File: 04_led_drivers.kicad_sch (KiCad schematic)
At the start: 22 parts, among them Q4 AO3401A (30V Vds, satisfies b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, Q5 AO3401A (30V Vds, satisfies b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, U5 LM3409HVMY/NOPB, U6 LM3409HVMY/NOPB

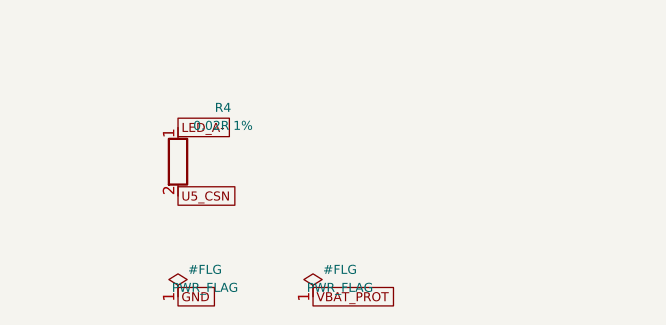
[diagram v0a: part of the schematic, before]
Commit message: Root sheet + full-hierarchy fixes (PWR_FLAG uniqueness, annotation, D-designator collision)
- red-light-panel.kicad_sch: 7 sheet symbols, no sheet-pins (global-label
  connectivity throughout, see docs/design_notes.md).
- tools/kicad_gen/fix_instance_paths.py: one-time pass populating each
  sub-sheet's per-symbol instances block with the real root-relative path
  (kicad-cli sch upgrade was silently emptying these -- invisible to ERC,
  but kicad-cli sch export bom flagged it as an annotation error).
- Fixed: multiple PWR_FLAGs on the same merged net conflicting with each
  other at full-hierarchy scale (now exactly one per net, project-wide);
  duplicate unnumbered '#FLG' references across sheets; a real
  reference-designator collision in the original BOM itself (D5-D68 LED
  range numerically includes D6/D7/D8, reused for sheet 6/7 parts --
  renumbered those three to D69/D70/D71).

Full-hierarchy 'kicad-cli sch erc' on the root sheet: 0 errors (157
cosmetic endpoint-off-grid warnings, 3 expected lib_symbol_mismatch
warnings from flattened extends-based parts). 'kicad-cli sch export bom':
153 rows, zero blank footprints, zero duplicate references, no
annotation warning.

Co-Authored-By: Claude Sonnet 5 <noreply@anthropic.com>
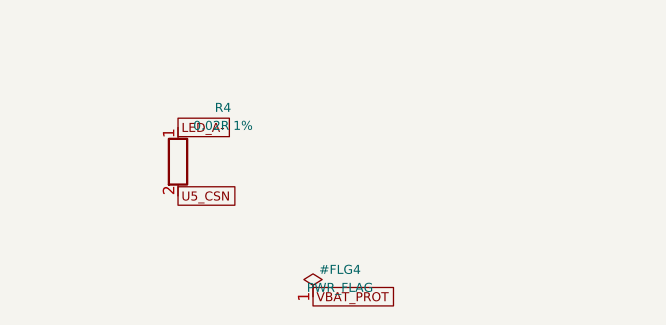
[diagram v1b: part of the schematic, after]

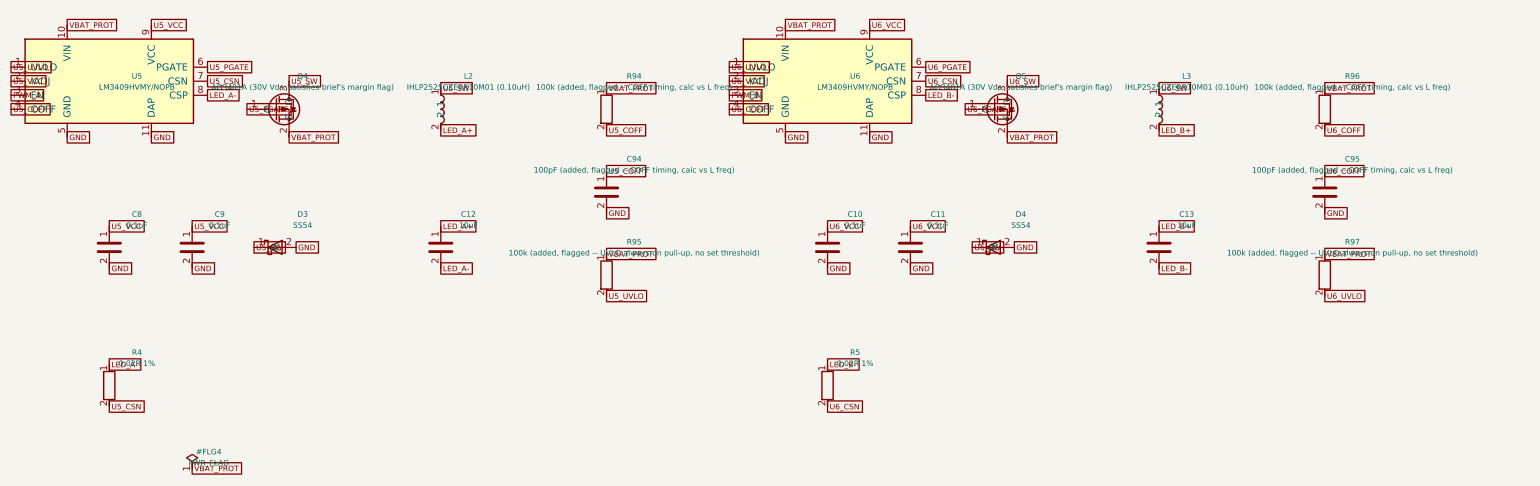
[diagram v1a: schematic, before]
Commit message: Schematic: replace global-label power nets with real power symbols
GND, VBAT, VBAT_PROT, 3V3, and USB_VBUS now get an actual KiCad power
symbol at every pin (power:GND, power:+3V3 with Value overridden to
'3V3', power:VBUS overridden to 'USB_VBUS', and two custom symbols for
VBAT/VBAT_PROT copied from stock power:+BATT into
libs/red-light-panel.kicad_sym) instead of a plain GlobalLabel -- the
idiomatic convention for power rails. All other cross-sheet signal nets
(I2C, PWM, LED channel outputs, etc.) remain GlobalLabels, which still
makes sense for data/PWM signals.

Confirmed empirically before rolling this out: overriding a stock power
symbol's Value does change its effective net name (power:+3V3 with
Value='3V3' correctly nets as '3V3'), and every power symbol's pin is
still power_in (never power_out), so existing PWR_FLAG placements are
unaffected. 0 ERC errors after the change; BOM still 153 components /
48 grouped rows, zero blank footprints, zero duplicate references.

Co-Authored-By: Claude Sonnet 5 <noreply@anthropic.com>
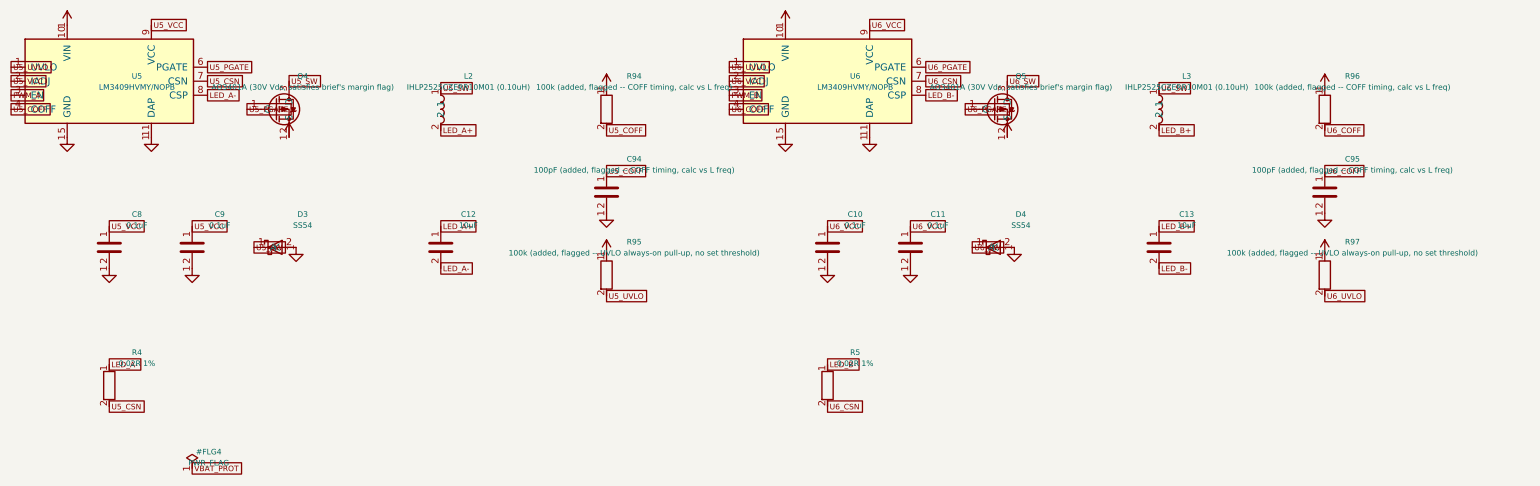
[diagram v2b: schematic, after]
